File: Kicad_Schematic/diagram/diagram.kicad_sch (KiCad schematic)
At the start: 10 parts, among them U1 Pico

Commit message: Finalized Kicad Schematic
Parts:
- added C1: .01 µF, symbol Device:C
- added LS1: Speaker, symbol Device:Speaker
- added R1: 1.6 kΩ, symbol Device:R
- added SW1, SW2, SW3: SW_Push, symbol Switch:SW_Push
- added SW4: SW_SPST, symbol Switch:SW_SPST
- added Speaker_Amplifier1: ~, symbol New_Library:Speaker_Amplifier
- added microphone: ~, symbol New_Library:microphone
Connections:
- net at addressable_led1. (GND), addressable_led2. (GND), addressable_led3. (GND): now also U1.29 (GPIO22); no longer U1.39 (VSYS), buck_converter. (Vout_(5V))
- net at U1.14 (GPIO10): now also SW1.2
- net at U1.15 (GPIO11): now also SW2.2
- net at U1.16 (GPIO12): now also SW3.2
- net at U1.17 (GPIO13): now also SW4.2 (B)
- net at U1.18 (GND): now also SW1.1, SW2.1, SW3.1, SW4.1 (A)
- net at U1.19 (GPIO14): now also microphone. (GND)
- net at U1.20 (GPIO15): now also microphone. (GND)
- net at U1.21 (GPIO16): now also microphone. (GND)
- net at U1.28 (GND): now also addressable_led1. (GND), addressable_led2. (GND), addressable_led3. (GND)
- net at U1.3 (GND): now also C1.1, Speaker_Amplifier1. (-)
- net at Adafruit_IMU1. (GND), U1.36 (3V3): now also microphone. (GND)
- net at U1.38 (GND): now also buck_converter. (Vout_(5V))
- net at U1.4 (GPIO2): now also R1.1
- net at Adafruit_IMU1. (GND), U1.42 (GND): now also microphone. (GND)
- removed net GND: addressable_led1. (GND), addressable_led2. (GND), addressable_led3. (GND), buck_converter. (Vout_(5V))
- new net: C1.2, R1.2, Speaker_Amplifier1. (-)
- new net: Speaker_Amplifier1. (-), U1.39 (VSYS), addressable_led1. (GND), addressable_led2. (GND), addressable_led3. (GND), buck_converter. (Vout_(5V))
- new net: LS1.1, Speaker_Amplifier1. (-)
- new net: LS1.2, Speaker_Amplifier1. (-)
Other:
- note added: "There will be 12 LEDs total"
- note removed: "There will be 12 LEDs in total"
- title: (none) -> ECE2799 Team 3 Circuit Schematic

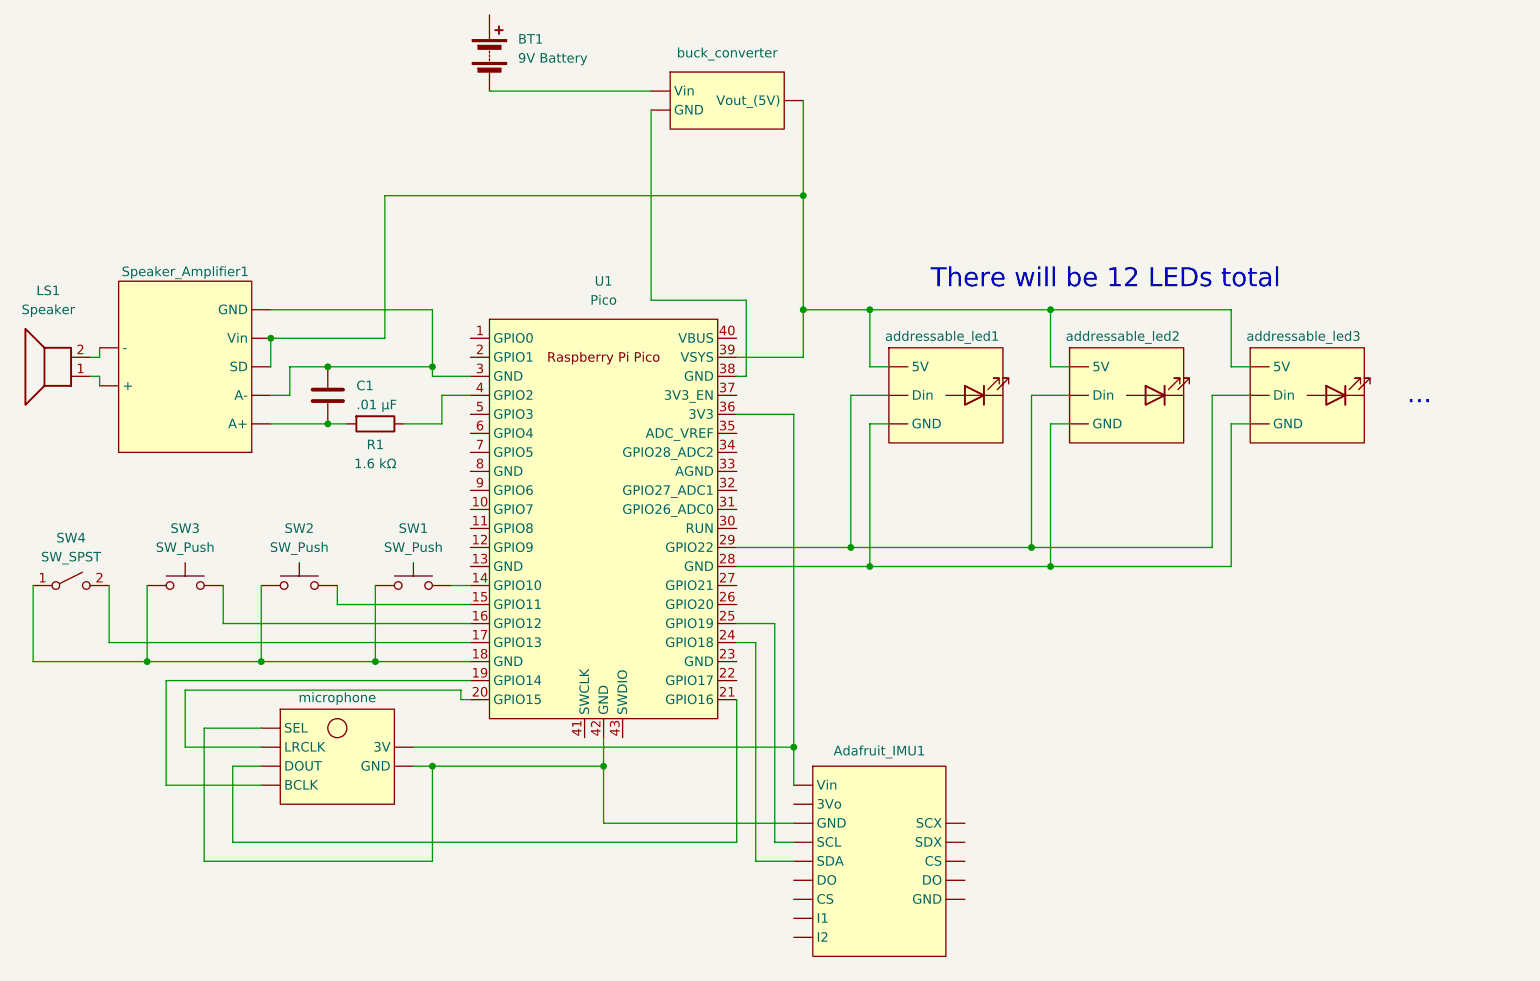
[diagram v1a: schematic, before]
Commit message: added inturrpt pins for IMU, added dataOut pin for LEDs
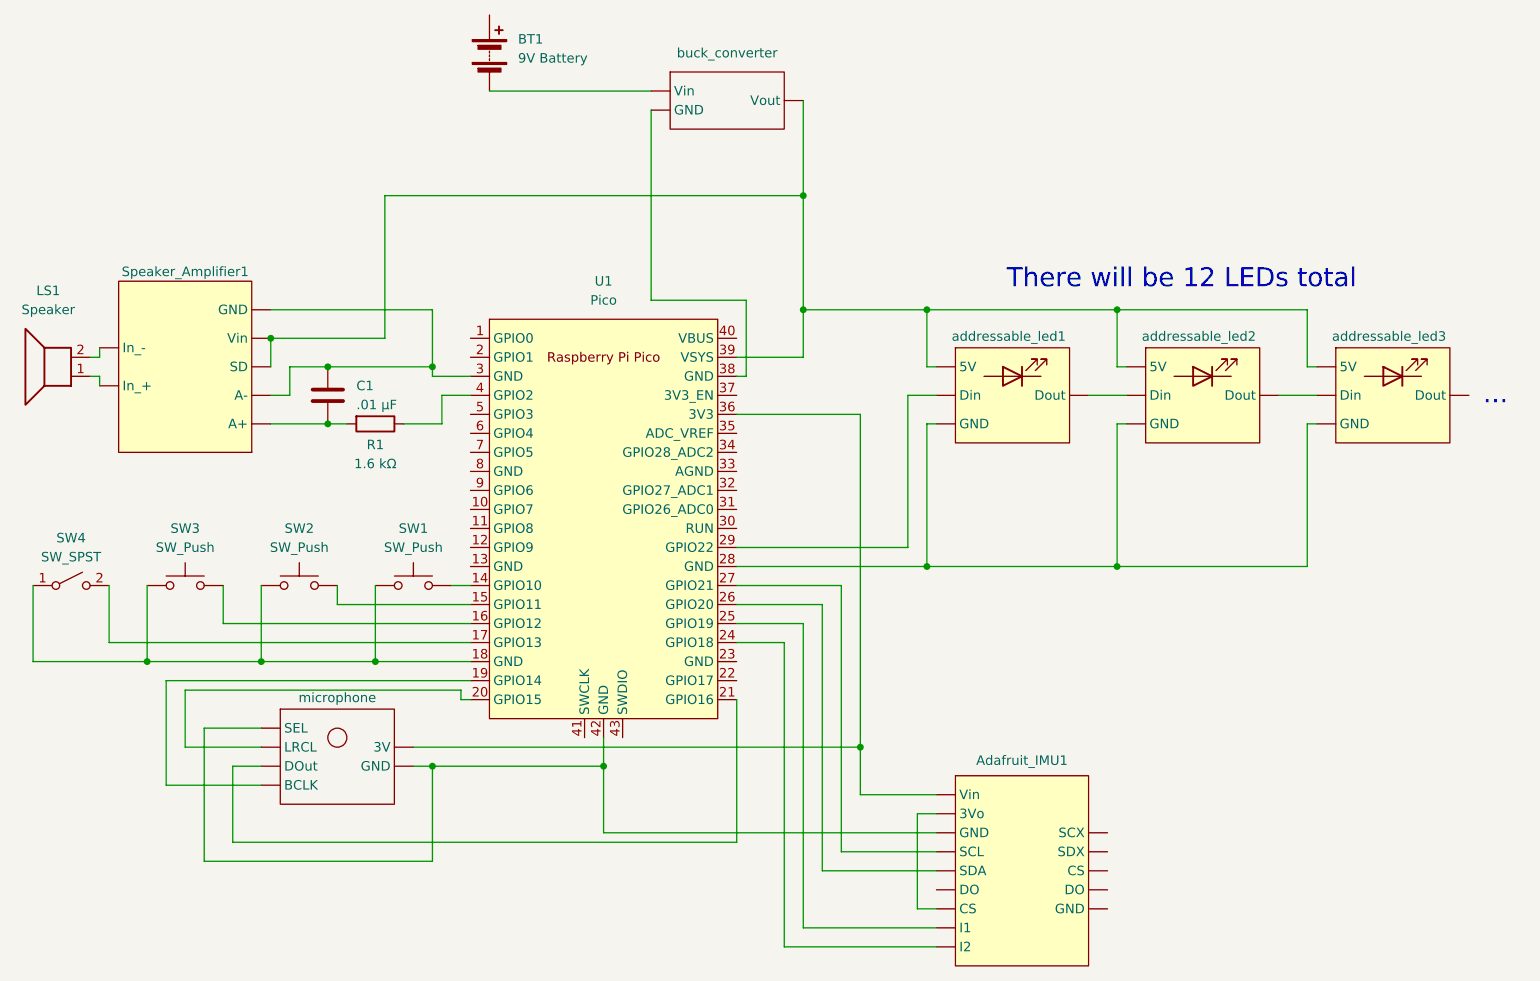
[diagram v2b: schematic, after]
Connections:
- net at U1.26 (GPIO20): now also Adafruit_IMU1. (GND)
- net at U1.27 (GPIO21): now also Adafruit_IMU1. (GND)
- new net: Speaker_Amplifier1. (In_-), U1.39 (VSYS), addressable_led1. (Dout), addressable_led2. (Dout), addressable_led3. (Dout), buck_converter. (Vout)
- new net: U1.28 (GND), addressable_led1. (Dout), addressable_led2. (Dout), addressable_led3. (Dout)
- new net: U1.29 (GPIO22), addressable_led1. (Dout)
- new net: Adafruit_IMU1. (GND), U1.36 (3V3), microphone. (GND)
- new net: addressable_led1. (Dout), addressable_led2. (Dout)
- new net: addressable_led2. (Dout), addressable_led3. (Dout)
- now unconnected: Adafruit_IMU1. (GND), addressable_led3. (GND), addressable_led3. (GND), addressable_led3. (GND)
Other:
- moved on the sheet: Adafruit_IMU1

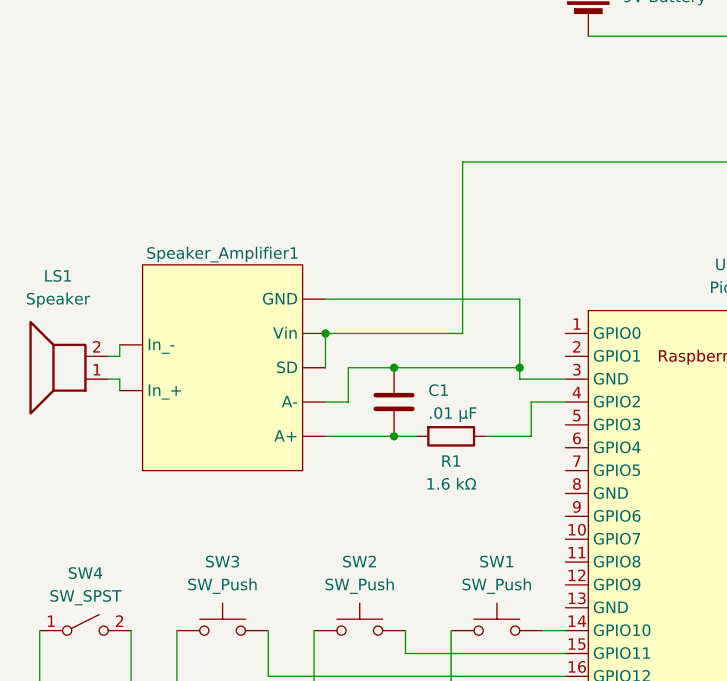
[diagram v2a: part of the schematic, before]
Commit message: edited block diagrams from design rev 2
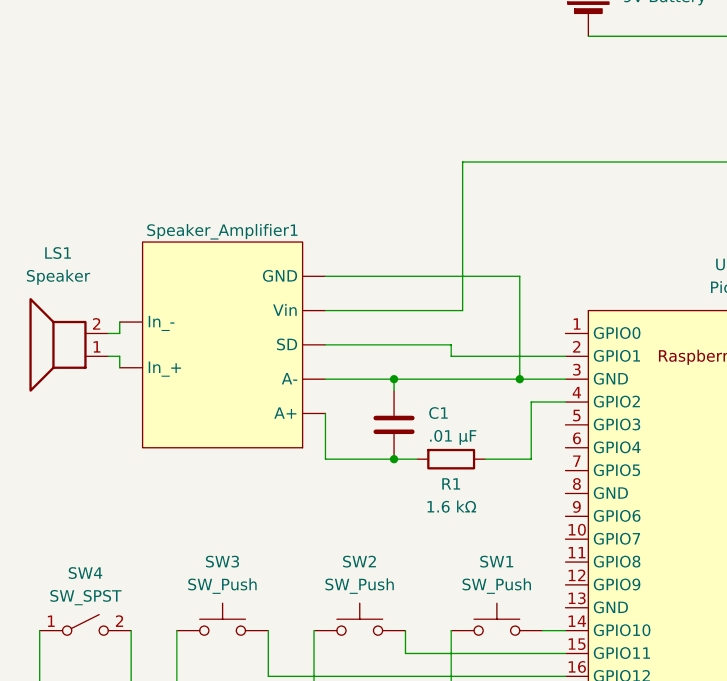
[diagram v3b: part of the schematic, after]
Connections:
- net at U1.2 (GPIO1): now also Speaker_Amplifier1. (In_-)
- new net: Speaker_Amplifier1. (In_-), U1.39 (VSYS), addressable_led1. (Dout), addressable_led2. (Dout), addressable_led3. (Dout), buck_converter. (Vout)
- new net: U1.28 (GND), addressable_led1. (Dout), addressable_led2. (Dout), addressable_led3. (Dout)
- new net: Adafruit_IMU1. (GND), U1.36 (3V3), microphone. (GND)
- now unconnected: Adafruit_IMU1. (GND), addressable_led3. (Dout), addressable_led3. (Dout)
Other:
- moved on the sheet: C1, LS1, R1, Speaker_Amplifier1
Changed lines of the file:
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@@
 	)
 	(junction
-		(at 71.12 69.85)
+		(at 85.09 71.12)
 		(diameter 0)
 		(color 0 0 0 0)
@@
 	)
 	(junction
+		(at 71.12 71.12)
+		(diameter 0)
+		(color 0 0 0 0)
+	)
+	(junction
 		(at 77.47 109.22)
 		(diameter 0)
@@
 	)
 	(junction
-		(at 71.12 77.47)
+		(at 71.12 80.01)
 		(diameter 0)
 		(color 0 0 0 0)
@@
 	)
 	(junction
-		(at 63.5 66.04)
-		(diameter 0)
-		(color 0 0 0 0)
-	)
-	(junction
 		(at 107.95 123.19)
 		(diameter 0)
@@
 		(color 0 0 0 0)
 	)
-	(junction
-		(at 85.09 69.85)
-		(diameter 0)
-		(color 0 0 0 0)
-	)
 	(wire
 		(pts
@@
 	(wire
 		(pts
-			(xy 66.04 73.66) (xy 66.04 69.85)
+			(xy 77.47 68.58) (xy 90.17 68.58)
 		)
 		(stroke
@@
 	(wire
 		(pts
-			(xy 63.5 77.47) (xy 71.12 77.47)
+			(xy 63.5 80.01) (xy 71.12 80.01)
 		)
 		(stroke
@@
 	(wire
 		(pts
-			(xy 63.5 66.04) (xy 63.5 69.85)
-		)
-		(stroke
-			(width 0)
-			(type default)
-		)
-	)
-	(wire
-		(pts
-			(xy 71.12 69.85) (xy 85.09 69.85)
+			(xy 71.12 71.12) (xy 85.09 71.12)
 		)
 		(stroke
@@
 	(wire
 		(pts
-			(xy 85.09 69.85) (xy 85.09 71.12)
+			(xy 63.5 67.31) (xy 77.47 67.31)
+		)
+		(stroke
+			(width 0)
+			(type default)
+		)
+	)
+	(wire
+		(pts
+			(xy 85.09 59.69) (xy 85.09 71.12)
 		)
 		(stroke
@@
 	(wire
 		(pts
+			(xy 77.47 67.31) (xy 77.47 68.58)
+		)
+		(stroke
+			(width 0)
+			(type default)
+		)
+	)
+	(wire
+		(pts
 			(xy 203.2 69.85) (xy 201.93 69.85)
 		)
@@
 	(wire
 		(pts
-			(xy 40.64 68.58) (xy 40.64 67.31)
+			(xy 40.64 66.04) (xy 40.64 64.77)
 		)
 		(stroke
@@
 	(wire
 		(pts
-			(xy 86.36 77.47) (xy 86.36 73.66)
+			(xy 86.36 80.01) (xy 86.36 73.66)
 		)
 		(stroke
@@
 	(wire
 		(pts
-			(xy 81.28 77.47) (xy 86.36 77.47)
+			(xy 81.28 80.01) (xy 86.36 80.01)
 		)
 		(stroke
@@
 	(wire
 		(pts
-			(xy 40.64 71.12) (xy 40.64 72.39)
+			(xy 40.64 68.58) (xy 40.64 69.85)
 		)
 		(stroke
@@
 	(wire
 		(pts
-			(xy 85.09 62.23) (xy 85.09 69.85)
-		)
-		(stroke
-			(width 0)
-			(type default)
-		)
-	)
-	(wire
-		(pts
-			(xy 66.04 69.85) (xy 71.12 69.85)
+			(xy 63.5 80.01) (xy 63.5 74.93)
+		)
+		(stroke
+			(width 0)
+			(type default)
+		)
+	)
+	(wire
+		(pts
+			(xy 71.12 72.39) (xy 71.12 71.12)
 		)
 		(stroke
@@
 	(wire
 		(pts
-			(xy 40.64 71.12) (xy 39.37 71.12)
+			(xy 40.64 68.58) (xy 39.37 68.58)
 		)
 		(stroke
@@
 	(wire
 		(pts
-			(xy 63.5 62.23) (xy 85.09 62.23)
+			(xy 63.5 59.69) (xy 85.09 59.69)
 		)
 		(stroke
@@
 	(wire
 		(pts
-			(xy 78.74 46.99) (xy 78.74 66.04)
+			(xy 78.74 46.99) (xy 78.74 63.5)
 		)
 		(stroke
@@
 	(wire
 		(pts
-			(xy 78.74 66.04) (xy 63.5 66.04)
+			(xy 78.74 63.5) (xy 63.5 63.5)
 		)
 		(stroke
@@
 	(wire
 		(pts
-			(xy 63.5 73.66) (xy 66.04 73.66)
+			(xy 63.5 71.12) (xy 71.12 71.12)
 		)
 		(stroke
@@
 	(wire
 		(pts
-			(xy 71.12 77.47) (xy 73.66 77.47)
+			(xy 71.12 80.01) (xy 73.66 80.01)
 		)
 		(stroke
@@
 	(wire
 		(pts
-			(xy 40.64 68.58) (xy 39.37 68.58)
+			(xy 40.64 66.04) (xy 39.37 66.04)
 		)
 		(stroke
@@
 	(symbol
 		(lib_id "Device:R")
-		(at 77.47 77.47 270)
+		(at 77.47 80.01 270)
 		(unit 1)
 		(exclude_from_sim no)
@@
 		(dnp no)
 		(property "Reference" "R1"
-			(at 77.47 80.264 90)
+			(at 77.47 82.804 90)
 			(effects
 				(font
@@
 		)
 		(property "Value" "1.6 kΩ"
-			(at 77.47 82.804 90)
+			(at 77.47 85.344 90)
 			(effects
 				(font
@@
 		)
 		(property "Footprint" ""
-			(at 77.47 75.692 90)
+			(at 77.47 78.232 90)
 			(effects
 				(font
@@
 		)
 		(property "Datasheet" "~"
-			(at 77.47 77.47 0)
+			(at 77.47 80.01 0)
 			(effects
 				(font
@@
 		)
 		(property "Description" "Resistor"
-			(at 77.47 77.47 0)
+			(at 77.47 80.01 0)
 			(effects
 				(font
@@
 	(symbol
 		(lib_id "Device:C")
-		(at 71.12 73.66 0)
+		(at 71.12 76.2 0)
 		(unit 1)
 		(exclude_from_sim no)
@@
 		(fields_autoplaced yes)
 		(property "Reference" "C1"
-			(at 74.93 72.3899 0)
+			(at 74.93 74.9299 0)
 			(effects
 				(font
@@
 		)
 		(property "Value" ".01 µF"
-			(at 74.93 74.9299 0)
+			(at 74.93 77.4699 0)
 			(effects
 				(font
@@
 		)
 		(property "Footprint" ""
-			(at 72.0852 77.47 0)
+			(at 72.0852 80.01 0)
 			(effects
 				(font
@@
 		)
 		(property "Datasheet" "~"
-			(at 71.12 73.66 0)
+			(at 71.12 76.2 0)
 			(effects
 				(font
@@
 		)
 		(property "Description" "Unpolarized capacitor"
-			(at 71.12 73.66 0)
+			(at 71.12 76.2 0)
 			(effects
 				(font
@@
 	(symbol
 		(lib_id "Device:Speaker")
-		(at 34.29 71.12 180)
+		(at 34.29 68.58 180)
 		(unit 1)
 		(exclude_from_sim no)
@@
 		(fields_autoplaced yes)
 		(property "Reference" "LS1"
+			(at 33.782 57.15 0)
+			(effects
+				(font
+					(size 1.27 1.27)
+				)
+			)
+		)
+		(property "Value" "Speaker"
 			(at 33.782 59.69 0)
 			(effects
@@
 			)
 		)
-		(property "Value" "Speaker"
-			(at 33.782 62.23 0)
-			(effects
-				(font
-					(size 1.27 1.27)
-				)
-			)
-		)
 		(property "Footprint" ""
-			(at 34.29 66.04 0)
+			(at 34.29 63.5 0)
 			(effects
 				(font
@@
 		)
 		(property "Datasheet" "~"
-			(at 34.544 69.85 0)
+			(at 34.544 67.31 0)
 			(effects
 				(font
@@
 		)
 		(property "Description" "Speaker"
-			(at 34.29 71.12 0)
+			(at 34.29 68.58 0)
 			(effects
 				(font
@@
 	(symbol
 		(lib_id "New_Library:Speaker_Amplifier")
-		(at 52.07 57.15 180)
+		(at 52.07 54.61 180)
 		(unit 1)
 		(exclude_from_sim no)
@@
 		(dnp no)
 		(property "Reference" "Speaker_Amplifier1"
-			(at 52.07 57.15 0)
+			(at 52.07 54.61 0)
 			(effects
 				(font
@@
 		)
 		(property "Value" "~"
-			(at 52.07 55.88 0)
+			(at 52.07 53.34 0)
 			(effects
 				(font
@@
 		)
 		(property "Footprint" ""
-			(at 52.07 57.15 0)
+			(at 52.07 54.61 0)
 			(effects
 				(font
@@
 		)
 		(property "Datasheet" ""
-			(at 52.07 57.15 0)
+			(at 52.07 54.61 0)
 			(effects
 				(font
@@
 		)
 		(property "Description" ""
-			(at 52.07 57.15 0)
-			(effects
-				(font
+			(at 52.07 54.61 0)
+			(effects
+				(font
